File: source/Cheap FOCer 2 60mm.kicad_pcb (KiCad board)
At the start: 2 copper layers, 59.1 x 99.9 mm, 228 parts, among them J1 Conn_01x02, J2 Conn_01x07, J3 Conn_01x03, J4 On/Off, J5 UNUSED MCU PINS, J6 Conn_01x03, P1 MOTOR1, P2 MOTOR1, P3 MOTOR1, P4 HALL/Encoder, P5 SWD, Q1 NCEP60T20, Q10 Q_PNP_BCE, Q11 Q_PNP_BCE, Q12 Q_PNP_BCE, Q2 NCEP60T20, Q3 NCEP60T20, Q4 NCEP60T20, Q5 NCEP60T20, Q6 NCEP60T20, Q7 Q_PNP_BCE, Q8 Q_PNP_BCE, Q9 Q_PNP_BCE, U1 AMS1117-3.3, U2 DRV8301, U3 TP2604-SR, U4 TJA1051T/3/1J, U5 STM32F405RGT6, U6 BMI160, X1 8MHz 10ppm (X50328MSB2GI)

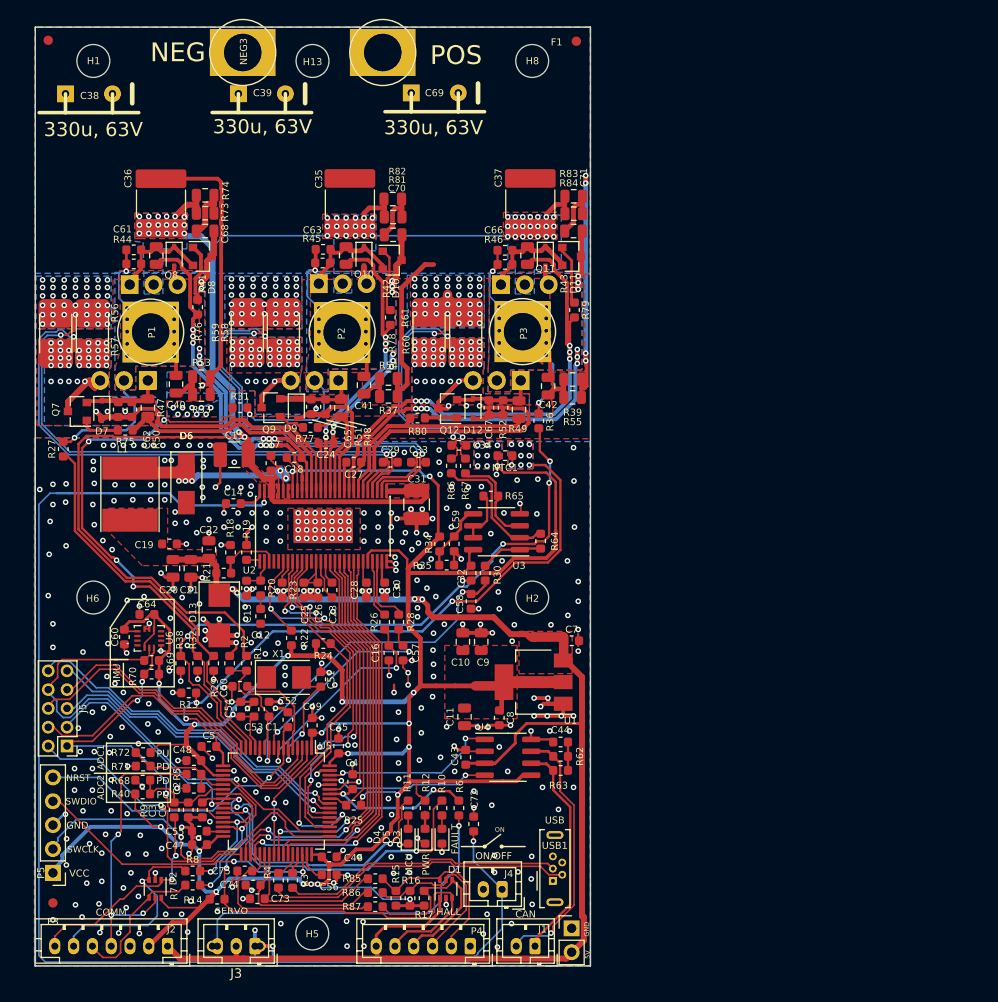
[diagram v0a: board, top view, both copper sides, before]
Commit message: Modified for OpenFFBoard.
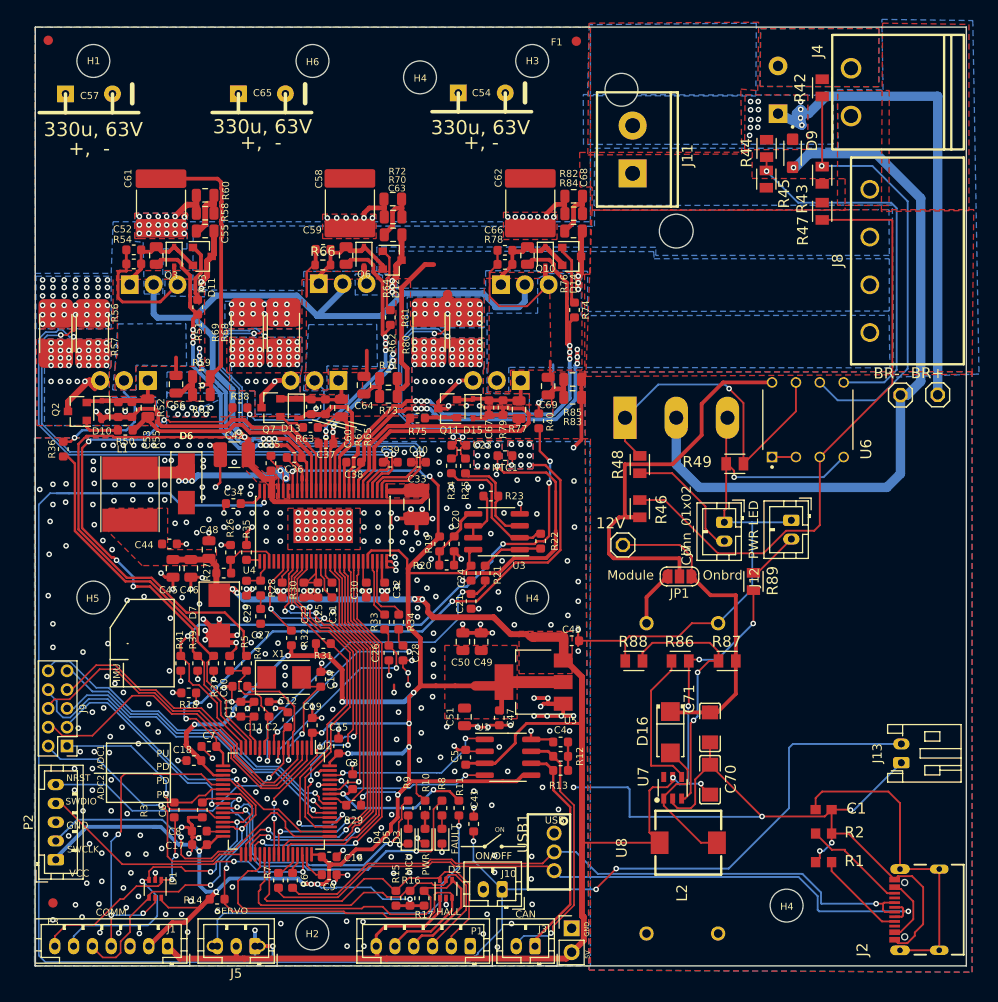
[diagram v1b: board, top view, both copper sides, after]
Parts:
- removed the C2 at (127.5, 150.0)
- removed the C3 at (126.9, 152.3)
- removed the C60 at (120.1, 133.9)
- removed the C64 at (122.5, 131.5)
- removed C73, C74, C75: 100n, Capacitor_SMD:C_0603_1608Metric
- removed NEG3: MOTOR3, CRF1:1pin_4mm
- removed the P1 at (122.9, 101.5)
- removed P3: MOTOR1, CRF1:1pin_4mm
- removed P5: SWD, Connector_PinHeader_2.54mm:PinHeader_1x05_P2.54mm_Vertical
- removed POS1: POS, CRF1:1pin_4mm
- removed the R40 at (122.0, 150.6)
- removed the R5 at (127.5, 148.5)
- removed the R68 at (122.1, 149.1)
- removed the R69 at (123.0, 136.4)
- removed the R7 at (127.4, 160.3)
- removed the R70 at (123.0, 137.8)
- removed the R71 at (122.1, 147.6)
- removed the R72 at (122.1, 146.2)
- removed the R8 at (127.4, 158.8)
- removed the R85 at (146.8, 159.6)
- added C1: 100nF, AppendLibrary:C0603, F.Cu at (194.5, 152.3)
- added C70: 22uF, AppendLibrary:C1206, F.Cu at (182.4, 149.1)
- added C71: 22uF, AppendLibrary:C1206, F.Cu at (182.4, 143.5)
- added D16: SS34, AppendLibrary:SMA_L4.3-W2.6-LS5.2-RD, F.Cu at (178.2, 144.0)
- added D8: STTH3010DTO-220AC_STM, Package_TO_SOT_THT:TO-220-2_Horizontal_TabUp, B.Cu at (189.7, 78.2)
- added D9: GOODWORK K110, VESC_OVP_Resistor_Schematic_v41:SODFL3618X110N, F.Cu at (191.2, 82.4)
- added H4: MountingHole, MountingHole:MountingHole_3.2mm_M3_ISO14580_Pad, F.Cu at (190.6, 162.5)
- added H4: MountingHole, MountingHole:MountingHole_3.2mm_M3_ISO14580_Pad, F.Cu at (151.6, 74.3)
- added J11: VESC_Vin, AppendLibrary:CONN-TH_1755736, F.Cu at (174.2, 82.0)
- added J12: PWR LED, Connector_JST:JST_PH_B2B-PH-K_1x02_P2.00mm_Vertical, F.Cu at (191.1, 121.5)
- added J13: E-Stop, Connector_JST:JST_PH_S2B-PH-K_1x02_P2.00mm_Horizontal, F.Cu at (202.8, 147.3)
- added J2: USB4105-GF-A, AppendLibrary:GCT_USB4105-GF-A, F.Cu at (206.8, 162.9)
- added J4: Conn_01x02, AppendLibrary:CONN-TH_2P-P5.08_1757242, F.Cu at (197.4, 75.9)
- added J7: Conn_01x02, Connector_JST:JST_PH_B2B-PH-K_1x02_P2.00mm_Vertical, F.Cu at (183.9, 121.7)
- added J8: MotorPower, AppendLibrary:CONN-TH_MSTBA2.5-4-G-5.08, F.Cu at (199.4, 93.9)
- added JP1: SolderJumper_3_Open, Jumper:SolderJumper-3_P1.3mm_Open_RoundedPad1.0x1.5mm_NumberLabels, F.Cu at (179.2, 127.5)
- added L2: 22uH, AppendLibrary:IND-SMD_L7.0-W6.8, F.Cu at (180.1, 155.8)
- added Q1: FGH40N60SFDTU, Package_TO_SOT_THT:TO-247-3_Horizontal_TabUp, B.Cu at (173.4, 110.6)
- added R1: 5.1k, AppendLibrary:R0603, F.Cu at (194.5, 157.9)
- added R2: 5.1k, AppendLibrary:R0603, F.Cu at (194.5, 154.8)
- added R42: 20k, VESC_OVP_Resistor_Schematic_v41:RESC2012X65, F.Cu at (194.4, 75.5)
- added R43: 1k, VESC_OVP_Resistor_Schematic_v41:RESC2012X65, F.Cu at (194.4, 84.8)
- added R44: 20k, VESC_OVP_Resistor_Schematic_v41:RESC2012X65, F.Cu at (188.4, 81.9)
- added R46: 10k, VESC_OVP_Resistor_Schematic_v41:RESC2012X65, F.Cu at (175.0, 120.2)
- added R47: 10k, VESC_OVP_Resistor_Schematic_v41:RESC2012X65, F.Cu at (194.4, 88.6)
- added R48: 560, VESC_OVP_Resistor_Schematic_v41:RESC2012X65, F.Cu at (175.0, 115.5)
- added R49: 10k, VESC_OVP_Resistor_Schematic_v41:RESC2012X65, F.Cu at (185.1, 115.5)
- added R66: 4.7k, Resistor_SMD:R_0603_1608Metric, F.Cu at (141.2, 94.3)
- added R88: 3k3, VESC_OVP_Resistor_Schematic_v41:RESC2012X65, F.Cu at (174.3, 136.4)
- added R89: 560, VESC_OVP_Resistor_Schematic_v41:RESC2012X65, F.Cu at (187.0, 128.0)
- added TP1: 12V, AppendLibrary:TP1X01, F.Cu at (173.2, 124.1)
- added TP2: BR-, AppendLibrary:TP1X01, F.Cu at (202.7, 108.2)
- added TP3: BR+, AppendLibrary:TP1X01, F.Cu at (206.7, 108.1)
- added U7: MT3608, AppendLibrary:SOT-23-6_L2.9-W1.6-P0.95-LS2.8-BL(MT3608), F.Cu at (178.5, 149.9)
- added U8: MT3608_Modle, AppendLibrary:MT3068_Module, F.Cu at (178.2, 147.7)
- P2: value MOTOR1 -> Conn_01x05_PH_SWIO; footprint CRF1:1pin_4mm -> Connector_JST:JST_PH_B5B-PH-K_1x05_P2.00mm_Vertical
- R3: renamed from R9; value 100R -> 0R
- R45: value 4.7k -> 1k; footprint Resistor_SMD:R_0603_1608Metric -> VESC_OVP_Resistor_Schematic_v41:RESC2012X65
- R56, R57: value 0.002R -> 0.01R
- R68: renamed from R58; value 0.002R -> 0.01R
- R69: renamed from R59; value 0.002R -> 0.01R
- R80: renamed from R60; value 0.002R -> 0.01R
- R81: renamed from R61; value 0.002R -> 0.01R
- R86: value 100R -> 10k; footprint Resistor_SMD:R_0603_1608Metric -> VESC_OVP_Resistor_Schematic_v41:RESC2012X65
- R87: value 100R -> 62K; footprint Resistor_SMD:R_0603_1608Metric -> VESC_OVP_Resistor_Schematic_v41:RESC2012X65
- U6: value BMI160 -> LM358P; footprint Package_LGA:Bosch_LGA-14_3x2.5mm_P0.5mm -> VESC_OVP_Resistor_Schematic_v41:DIP794W45P254L959H508Q8
- USB1: value USB Micro U-D-M5DD-W-1 -> Conn_01x03; footprint Connector_USB:USB_Micro-B_Wuerth_614105150721_Vertical -> AppendLibrary:CONN-TH_B3B-PH-K-S
- moved U6 73.8 mm to (192.8, 110.8), turned to 90 degrees
- moved P2 63.8 mm to (112.8, 157.6)
- moved R45 48.1 mm to (188.4, 85.2), turned to 90 degrees
- moved R87 45.7 mm to (184.3, 136.4)
- moved R86 40.7 mm to (179.2, 136.4)
- moved C54 5.00 mm to (157.4, 77.3)
- moved USB1 3.08 mm to (165.8, 156.8)
- renumbered C50 to C10, C53 to C11, C52 to C12, C54 to C13, C51 to C14, C45 to C15, C46 to C16, C47 to C17, C48 to C18, C49 to C19, C1 to C2, C59 to C20, C58 to C21, C25 to C22, C34 to C23, C32 to C24, C26 to C25, C16 to C26, C12 to C27, C57 to C28, C13 to C29, C4 to C3, C28 to C30, C23 to C31, C30 to C32, C31 to C33, C14 to C34, C17 to C35, C18 to C36, C24 to C37, C27 to C38, C29 to C39, C44 to C4, C33 to C40, C72 to C41, C15 to C42, C7 to C43, C19 to C44, C20 to C45, C21 to C46, C8 to C47, C22 to C48, C9 to C49, C43 to C5, C10 to C50, C11 to C51, C61 to C52, C62 to C53, C69 to C54, C68 to C55, C40 to C56, C38 to C57, C35 to C58, C63 to C59, C65 to C60, C36 to C61, C37 to C62, C70 to C63, C41 to C64, C39 to C65, C71 to C68, C42 to C69, C5 to C7, C55 to C8, C56 to C9, D2 to D1, D7 to D10, D8 to D11, D10 to D12, D9 to D13, D11 to D14, D12 to D15, D1 to D2, D13 to D7, H5 to H2, H8 to H3, H2 to H4, H6 to H5, H13 to H6, H3 to H7, H4 to H8, J2 to J1, J4 to J10, J1 to J3, J3 to J5, J5 to J9, NT4 to NT2, NT2 to NT3, NT5 to NT4, NT3 to NT5, P4 to P1, Q11 to Q10, Q12 to Q11, Q3 to Q12, Q6 to Q13, Q7 to Q2, Q8 to Q3, Q1 to Q4, Q4 to Q5, Q10 to Q6, Q9 to Q7, Q2 to Q8, Q5 to Q9, R12 to R10, R6 to R11, R62 to R12, R63 to R13, R13 to R18, R34 to R19, R35 to R20, R30 to R21, R64 to R22, R65 to R23, R66 to R24, R67 to R25, R18 to R26, R21 to R27, R20 to R28, R25 to R29, R23 to R30, R24 to R31, R22 to R32, R26 to R33, R28 to R34, R19 to R35, R27 to R36, R29 to R37, R31 to R38, R32 to R39, R1 to R4, R36 to R40, R38 to R41, R2 to R5, R75 to R50, R76 to R51, R47 to R52, R41 to R53, R44 to R54, R50 to R55, R73 to R58, R53 to R59, R3 to R6, R74 to R60, R33 to R61, R78 to R62, R77 to R63, R42 to R64, R48 to R65, R51 to R67, R4 to R7, R81 to R70, R54 to R71, R82 to R72, R37 to R73, R79 to R74, R80 to R75, R43 to R76, R49 to R77, R46 to R78, R52 to R79, R10 to R8, R83 to R82, R55 to R83, R39 to R85, R11 to R9, U4 to U1, U5 to U2, U2 to U4, U1 to U5
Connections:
- C59 pad 1: Net-(C63-Pad1) -> Net-(D12-K)
- D12 pad 1: Net-(C63-Pad1) -> Net-(D12-K)
- D2 pad 6: /Filters/HALL3_IN -> /HALL3
- P1 pad 2: /Filters/HALL3_IN -> /HALL3
- P2 pad 1: /Mosfet driver/H2_VS -> VCC
- Q6 pad 2: Net-(C63-Pad1) -> Net-(D12-K)
- Q8 pad 1: Net-(C63-Pad1) -> Net-(D12-K)
- R15 pad 1: /Filters/HALL3_IN -> /HALL3
- R45 pad 1: /Mosfet driver/H2_VS -> GND
- R45 pad 2: Net-(C63-Pad1) -> /OverVoltageProtector/+IN2
- R6 pad 2: Net-(R3-Pad2) -> Net-(J2-DP1)
- R64 pad 1: Net-(C63-Pad1) -> Net-(D12-K)
- R7 pad 2: Net-(R4-Pad2) -> Net-(J2-DN1)
- R86 pad 1: /Filters/HALL2_OUT -> Net-(U7-EN)
- R86 pad 2: /Filters/HALL2_IN -> +5V
- R87 pad 1: /Filters/HALL1_OUT -> Net-(U7-FB)
- R87 pad 2: /Filters/HALL1_IN -> /12VBoost/VOUT+
- U2 pad 20: /MCU/RX_SDA_NSS -> /RX_SDA_IN
- U2 pad 21: /MCU/SCK_ADC_EXT -> /SCK_ADC_EXT_IN
- U2 pad 23: /MCU/TX_SCL_MOSI -> /TX_SCL_MOSI_IN
- U2 pad 29: /MCU/TX_SCL_MOSI -> /TX_SCL_MOSI_IN
- U2 pad 30: /MCU/RX_SDA_NSS -> /RX_SDA_IN
- U2 pad 37: /Filters/HALL1_OUT -> /Filters/HALL1_IN
- U2 pad 38: /Filters/HALL2_OUT -> /Filters/HALL2_IN
- U4 pad 12: Net-(U2-Pad12) -> unconnected-(U4-DC_CAL-Pad12)
- U4 pad 4: Net-(U2-Pad4) -> unconnected-(U4-PWRGD-Pad4)
- U4 pad 5: Net-(U2-Pad5) -> unconnected-(U4-OCTW-Pad5)
- U6 pad 1: GND -> Net-(U6A--IN1)
- U6 pad 2: Net-(U6-Pad2) -> Net-(U6A--IN1)
- U6 pad 4: Net-(U6-Pad4) -> GND
- U6 pad 5: VCC -> /OverVoltageProtector/+IN2
- U6 pad 6: GND -> /OverVoltageProtector/-IN2
- U6 pad 7: GND -> /OverVoltageProtector/OUT2
- U6 pad 8: VCC -> /OverVoltageProtector/12V
- USB1 pad 1: Net-(USB1-Pad1) -> GND
- USB1 pad 2: Net-(R4-Pad2) -> Net-(J2-DP1)
- USB1 pad 3: Net-(R3-Pad2) -> Net-(J2-DN1)
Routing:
- net GND: track 267.1 -> 384.7 mm, vias 510 -> 448
- net /OverVoltageProtector/BRAKE_RTN: track 0.00 -> 77.2 mm, vias 0 -> 1
- net Net-(J2-DN1): track 0.00 -> 75.5 mm, vias 0 -> 1
- net Net-(J2-DP1): track 0.00 -> 71.6 mm, vias 0 -> 1
- net Net-(U6A-+IN1): track 0.00 -> 65.9 mm
- net V_SUPPLY: track 157.5 -> 219.4 mm, vias 59 -> 46
- net Net-(J10-A): track 137.1 -> 189.9 mm, vias 2 -> 4
- net +5V: track 174.6 -> 222.6 mm, vias 4 -> 9
- net /OverVoltageProtector/-IN2: track 0.00 -> 47.5 mm, vias 0 -> 1
- net /OverVoltageProtector/12V: track 0.00 -> 44.7 mm
- net VCC: track 346.3 -> 304.1 mm, vias 29 -> 27
- net /OverVoltageProtector/+IN2: track 0.00 -> 40.3 mm, vias 0 -> 1
- net /OverVoltageProtector/OUT2: track 0.00 -> 37.0 mm, vias 0 -> 1
- net Net-(C1-Pad1): track 0.00 -> 35.0 mm
- net /12VBoost/VOUT+: track 0.00 -> 33.9 mm
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- added copper zone on B.Cu, net /48Vin
- added copper zone on F.Cu, net /48Vin
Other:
- board size 59.1 x 99.9 mm -> 99.1 x 99.9 mm
- net class Default removed
- board text added: "48v"
- board text added: "U"
- board text added: "V"
- board text added: "W"
- board text removed: "NEG"
- board text removed: "POS"
